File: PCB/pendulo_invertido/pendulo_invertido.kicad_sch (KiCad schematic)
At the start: 6 parts, among them U1 ESP32-DevKitC V4, U2 MPU6050, U3 TB6612FNG, U5 L7805

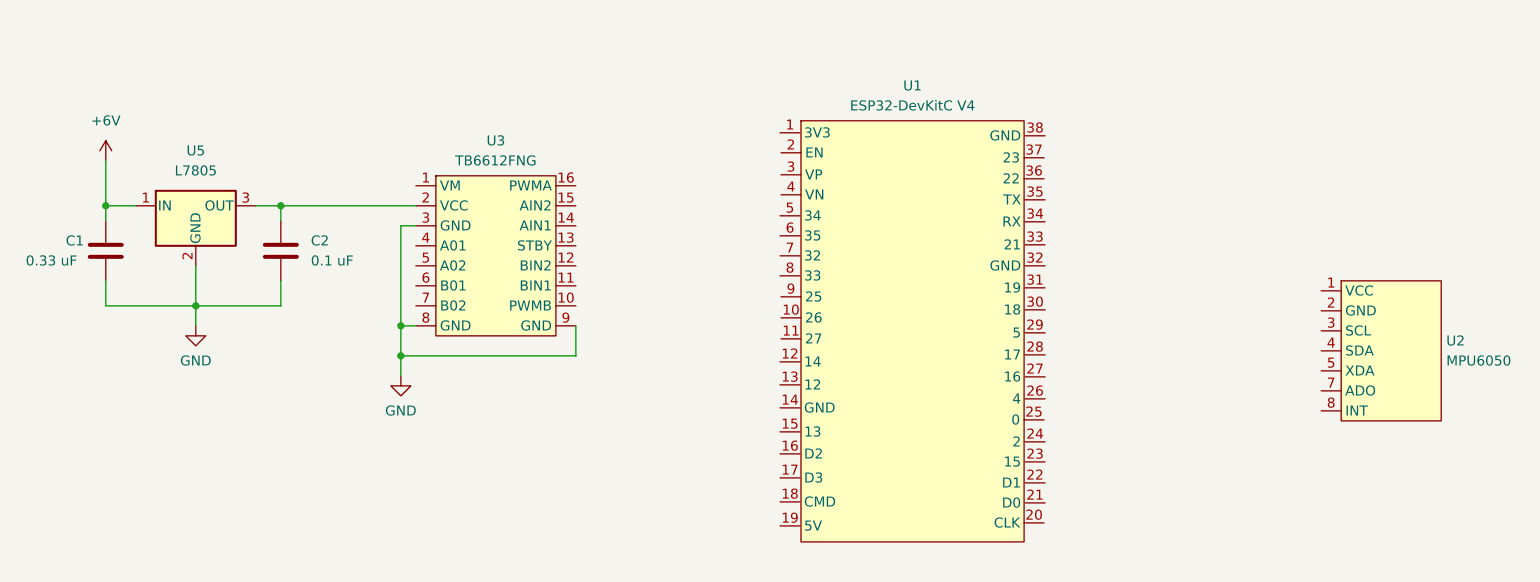
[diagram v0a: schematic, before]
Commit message: Cambios en el esquematico
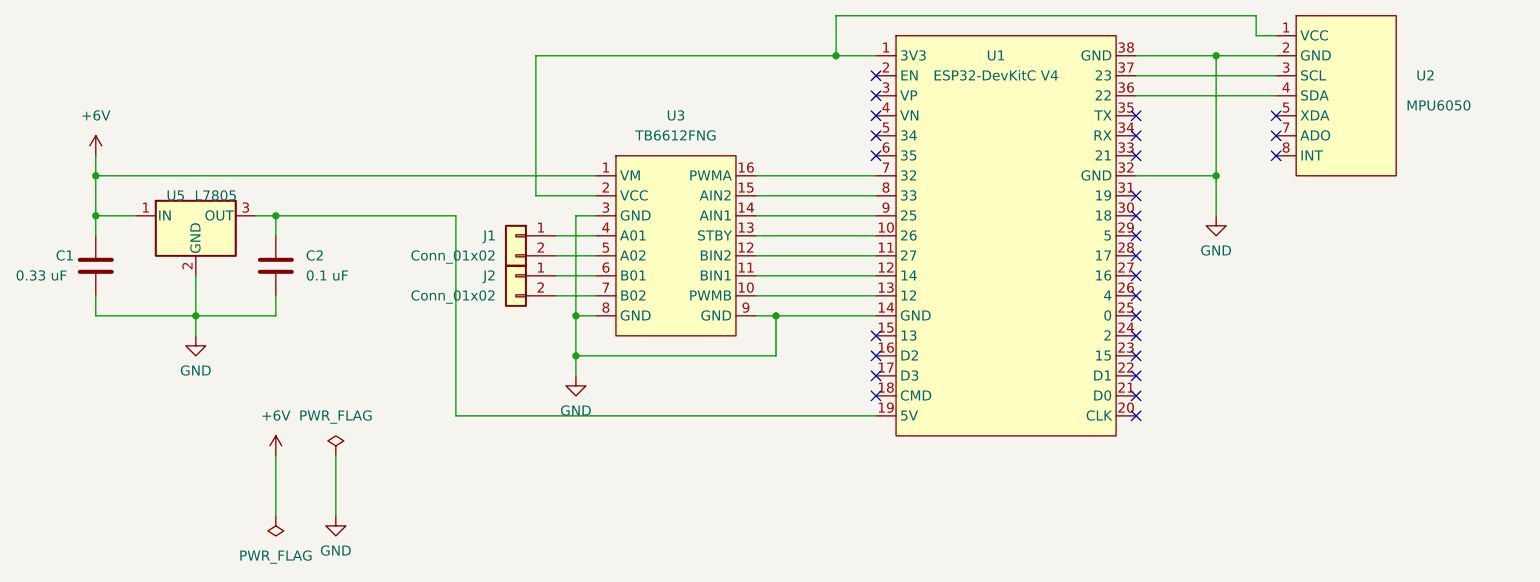
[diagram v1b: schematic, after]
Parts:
- added J1, J2: Conn_01x02, Connector_JST:JST_XH_B2B-XH-A_1x02_P2.50mm_Vertical, symbol Connector_Generic:Conn_01x02
- U1: footprint (none) -> PCM_Espressif:ESP32-DevKitC
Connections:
- net +6V: now also U3.1 (VM)
- net GND: now also U1.14 (GND), U1.32 (GND), U1.38 (GND), U2.2 (GND)
- net at U3.10 (PWMB): now also U1.13 (12)
- net at U3.11 (BIN1): now also U1.12 (14)
- net at U3.12 (BIN2): now also U1.11 (27)
- net at U3.13 (STBY): now also U1.10 (26)
- net at U3.14 (AIN1): now also U1.9 (25)
- net at U3.15 (AIN2): now also U1.8 (33)
- net at U3.16 (PWMA): now also U1.7 (32)
- net at C2.1, U5.3 (OUT): now also U1.19 (5V); no longer U3.2 (VCC)
- net at U3.4 (A01): now also J1.1 (Pin_1)
- net at U3.5 (A02): now also J1.2 (Pin_2)
- net at U3.6 (B01): now also J2.1 (Pin_1)
- net at U3.7 (B02): now also J2.2 (Pin_2)
- net at U1.1 (3V3): now also U2.1 (VCC), U3.2 (VCC)
- net at U1.36 (22): now also U2.4 (SDA)
- net at U1.37 (23): now also U2.3 (SCL)
- no-connect marks 0 -> 27
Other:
- moved on the sheet: C1, C2, U5

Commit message: prototipo diseño PCB
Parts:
- C1: value 0.33 uF -> 0.1 uF; footprint (none) -> Capacitor_THT:C_Disc_D4.7mm_W2.5mm_P5.00mm
- C2: footprint (none) -> Capacitor_THT:C_Disc_D4.7mm_W2.5mm_P5.00mm
- U2: footprint (none) -> pendulo_invertido:MPU6050
- U3: footprint (none) -> pendulo_invertido:TB6612FNG
- U5: footprint (none) -> Package_TO_SOT_THT:TO-220-3_Horizontal_TabDown
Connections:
- no-connect marks 27 -> 28
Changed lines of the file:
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@@
   (no_connect (at 172.72 76.2))
   (no_connect (at 172.72 66.04))
+  (no_connect (at 190.5 63.5))
   (no_connect (at 139.7 86.36))
   (no_connect (at 139.7 50.8))
@@
       (effects (font (size 1.27 1.27)))
     )
-    (property "Footprint" "" (at 106.68 60.96 0)
+    (property "Footprint" "pendulo_invertido:TB6612FNG" (at 106.68 60.96 0)
       (effects (font (size 1.27 1.27)) hide)
     )
@@
   )
   (symbol (lib_id "P_I:MPU6050") (at 193.04 43.18 0) (unit 1)
-    (in_bom yes) (on_board yes) (dnp no)
-    (property "Reference" "U2" (at 208.28 50.8 0)
-      (effects (font (size 1.27 1.27)) (justify left))
-    )
-    (property "Value" "MPU6050" (at 207.01 54.61 0)
-      (effects (font (size 1.27 1.27)) (justify left))
-    )
-    (property "Footprint" "" (at 193.04 43.18 0)
+    (in_bom yes) (on_board yes) (dnp no) (fields_autoplaced)
+    (property "Reference" "U2" (at 207.01 53.34 0)
+      (effects (font (size 1.27 1.27)) (justify left))
+    )
+    (property "Value" "MPU6050" (at 207.01 55.88 0)
+      (effects (font (size 1.27 1.27)) (justify left))
+    )
+    (property "Footprint" "pendulo_invertido:MPU6050" (at 193.04 43.18 0)
       (effects (font (size 1.27 1.27)) hide)
     )
@@
     (pin "4")
     (pin "5")
+    (pin "6")
     (pin "7")
     (pin "8")
@@
       (effects (font (size 1.27 1.27)) (justify left))
     )
-    (property "Footprint" "" (at 64.4652 78.74 0)
+    (property "Footprint" "Capacitor_THT:C_Disc_D4.7mm_W2.5mm_P5.00mm" (at 64.4652 78.74 0)
       (effects (font (size 1.27 1.27)) hide)
     )
@@
         (path "/7f26cb57-504d-41bd-9858-402af83d29a6"
           (reference "#PWR04") (unit 1)
+        )
+      )
+    )
+  )
+  (symbol (lib_id "Device:C") (at 40.64 74.93 0) (unit 1)
+    (in_bom yes) (on_board yes) (dnp no) (fields_autoplaced)
+    (property "Reference" "C1" (at 44.45 73.66 0)
+      (effects (font (size 1.27 1.27)) (justify left))
+    )
+    (property "Value" "0.1 uF" (at 44.45 76.2 0)
+      (effects (font (size 1.27 1.27)) (justify left))
+    )
+    (property "Footprint" "Capacitor_THT:C_Disc_D4.7mm_W2.5mm_P5.00mm" (at 41.6052 78.74 0)
+      (effects (font (size 1.27 1.27)) hide)
+    )
+    (property "Datasheet" "~" (at 40.64 74.93 0)
+      (effects (font (size 1.27 1.27)) hide)
+    )
+    (pin "1")
+    (pin "2")
+    (instances
+      (project "pendulo_invertido"
+        (path "/7f26cb57-504d-41bd-9858-402af83d29a6"
+          (reference "C1") (unit 1)
         )
       )
@@
       (effects (font (size 1.27 1.27)))
     )
-    (property "Footprint" "" (at 53.975 72.39 0)
+    (property "Footprint" "Package_TO_SOT_THT:TO-220-3_Horizontal_TabDown" (at 53.975 72.39 0)
       (effects (font (size 1.27 1.27) italic) (justify left) hide)
     )
@@
         )
       )
-    )
-  )
-  (symbol (lib_id "Device:C") (at 40.64 74.93 0) (unit 1)
-    (in_bom yes) (on_board yes) (dnp no)
-    (property "Reference" "C1" (at 35.56 73.66 0)
-      (effects (font (size 1.27 1.27)) (justify left))
-    )
-    (property "Value" "0.33 uF" (at 30.48 76.2 0)
-      (effects (font (size 1.27 1.27)) (justify left))
-    )
-    (property "Footprint" "" (at 41.6052 78.74 0)
-      (effects (font (size 1.27 1.27)) hide)
-    )
-    (property "Datasheet" "~" (at 40.64 74.93 0)
-      (effects (font (size 1.27 1.27)) hide)
-    )
-    (pin "1")
-    (pin "2")
-    (instances
-      (project "pendulo_invertido"
-        (path "/7f26cb57-504d-41bd-9858-402af83d29a6"
-          (reference "C1") (unit 1)
-        )
-      )

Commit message: modificaciones prototipo
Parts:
- C1: value 0.1 uF -> 0.33 uF; footprint Capacitor_THT:C_Disc_D4.7mm_W2.5mm_P5.00mm -> Capacitor_THT:C_Radial_D5.0mm_H11.0mm_P2.00mm
- C2: footprint Capacitor_THT:C_Disc_D4.7mm_W2.5mm_P5.00mm -> Capacitor_THT:C_Radial_D5.0mm_H11.0mm_P2.00mm
- U5: footprint Package_TO_SOT_THT:TO-220-3_Horizontal_TabDown -> Package_TO_SOT_THT:TO-220-3_Vertical
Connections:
- net at U2.3 (SCL): now also U1.17 (D3); no longer U1.37 (23)
- net at U2.4 (SDA): now also U1.16 (D2); no longer U1.36 (22)
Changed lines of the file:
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@@
   (no_connect (at 139.7 53.34))
   (no_connect (at 172.72 88.9))
+  (no_connect (at 172.72 50.8))
   (no_connect (at 172.72 55.88))
   (no_connect (at 172.72 58.42))
@@
   (no_connect (at 172.72 66.04))
   (no_connect (at 190.5 63.5))
-  (no_connect (at 139.7 86.36))
+  (no_connect (at 139.7 83.82))
   (no_connect (at 139.7 50.8))
   (no_connect (at 172.72 93.98))
@@
   (no_connect (at 172.72 68.58))
   (no_connect (at 139.7 60.96))
-  (no_connect (at 139.7 83.82))
-  (no_connect (at 139.7 88.9))
   (no_connect (at 139.7 91.44))
   (no_connect (at 172.72 60.96))
+  (no_connect (at 172.72 53.34))
   (no_connect (at 190.5 60.96))
   (no_connect (at 172.72 91.44))
+  (wire (pts (xy 187.96 53.34) (xy 190.5 53.34))
+    (stroke (width 0) (type default))
+  )
+  (wire (pts (xy 185.42 50.8) (xy 190.5 50.8))
+    (stroke (width 0) (type default))
+  )
   (wire (pts (xy 190.5 45.72) (xy 187.96 45.72))
     (stroke (width 0) (type default))
   )
+  (wire (pts (xy 187.96 101.6) (xy 187.96 53.34))
+    (stroke (width 0) (type default))
+  )
   (wire (pts (xy 182.88 48.26) (xy 182.88 63.5))
     (stroke (width 0) (type default))
@@
     (stroke (width 0) (type default))
   )
-  (wire (pts (xy 172.72 50.8) (xy 190.5 50.8))
-    (stroke (width 0) (type default))
-  )
   (wire (pts (xy 124.46 81.28) (xy 127 81.28))
     (stroke (width 0) (type default))
@@
     (stroke (width 0) (type default))
   )
+  (wire (pts (xy 134.62 86.36) (xy 134.62 101.6))
+    (stroke (width 0) (type default))
+  )
   (wire (pts (xy 124.46 71.12) (xy 139.7 71.12))
     (stroke (width 0) (type default))
@@
     (stroke (width 0) (type default))
   )
+  (wire (pts (xy 139.7 88.9) (xy 137.16 88.9))
+    (stroke (width 0) (type default))
+  )
   (wire (pts (xy 134.62 48.26) (xy 96.52 48.26))
     (stroke (width 0) (type default))
   )
+  (wire (pts (xy 185.42 99.06) (xy 185.42 50.8))
+    (stroke (width 0) (type default))
+  )
   (wire (pts (xy 182.88 48.26) (xy 190.5 48.26))
     (stroke (width 0) (type default))
@@
     (stroke (width 0) (type default))
   )
+  (wire (pts (xy 137.16 88.9) (xy 137.16 99.06))
+    (stroke (width 0) (type default))
+  )
   (wire (pts (xy 86.36 68.58) (xy 63.5 68.58))
     (stroke (width 0) (type default))
@@
     (stroke (width 0) (type default))
   )
+  (wire (pts (xy 137.16 99.06) (xy 185.42 99.06))
+    (stroke (width 0) (type default))
+  )
   (wire (pts (xy 40.64 68.58) (xy 45.72 68.58))
     (stroke (width 0) (type default))
@@
     (stroke (width 0) (type default))
   )
+  (wire (pts (xy 134.62 101.6) (xy 187.96 101.6))
+    (stroke (width 0) (type default))
+  )
+  (wire (pts (xy 139.7 86.36) (xy 134.62 86.36))
+    (stroke (width 0) (type default))
+  )
   (wire (pts (xy 96.52 48.26) (xy 96.52 66.04))
     (stroke (width 0) (type default))
@@
   )
   (wire (pts (xy 60.96 68.58) (xy 63.5 68.58))
-    (stroke (width 0) (type default))
-  )
-  (wire (pts (xy 172.72 53.34) (xy 190.5 53.34))
     (stroke (width 0) (type default))
   )
@@
       (effects (font (size 1.27 1.27)) (justify left))
     )
-    (property "Footprint" "Capacitor_THT:C_Disc_D4.7mm_W2.5mm_P5.00mm" (at 64.4652 78.74 0)
+    (property "Footprint" "Capacitor_THT:C_Radial_D5.0mm_H11.0mm_P2.00mm" (at 64.4652 78.74 0)
       (effects (font (size 1.27 1.27)) hide)
     )
@@
       (effects (font (size 1.27 1.27)) (justify left))
     )
-    (property "Value" "0.1 uF" (at 44.45 76.2 0)
-      (effects (font (size 1.27 1.27)) (justify left))
-    )
-    (property "Footprint" "Capacitor_THT:C_Disc_D4.7mm_W2.5mm_P5.00mm" (at 41.6052 78.74 0)
+    (property "Value" "0.33 uF" (at 44.45 76.2 0)
+      (effects (font (size 1.27 1.27)) (justify left))
+    )
+    (property "Footprint" "Capacitor_THT:C_Radial_D5.0mm_H11.0mm_P2.00mm" (at 41.6052 78.74 0)
       (effects (font (size 1.27 1.27)) hide)
     )
@@
       (effects (font (size 1.27 1.27)))
     )
-    (property "Footprint" "Package_TO_SOT_THT:TO-220-3_Horizontal_TabDown" (at 53.975 72.39 0)
+    (property "Footprint" "Package_TO_SOT_THT:TO-220-3_Vertical" (at 53.975 72.39 0)
       (effects (font (size 1.27 1.27) italic) (justify left) hide)
     )
